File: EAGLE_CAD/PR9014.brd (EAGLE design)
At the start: 68.1 x 70.2 mm, 69 parts, among them J1 M3_SCREW_POST, SW1 C&K_PTS645

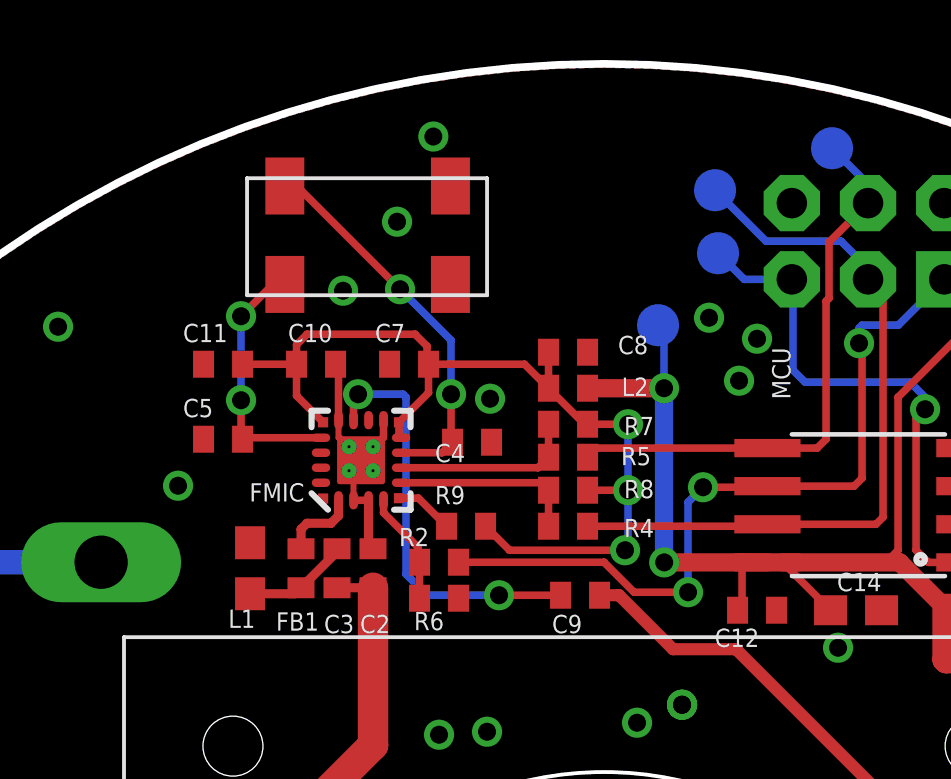
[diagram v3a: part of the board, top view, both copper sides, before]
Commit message: minor ish changes
relative to my last commit, at least

one thing that mattered a little is that i changed the XTAL package -
it was off a bit.
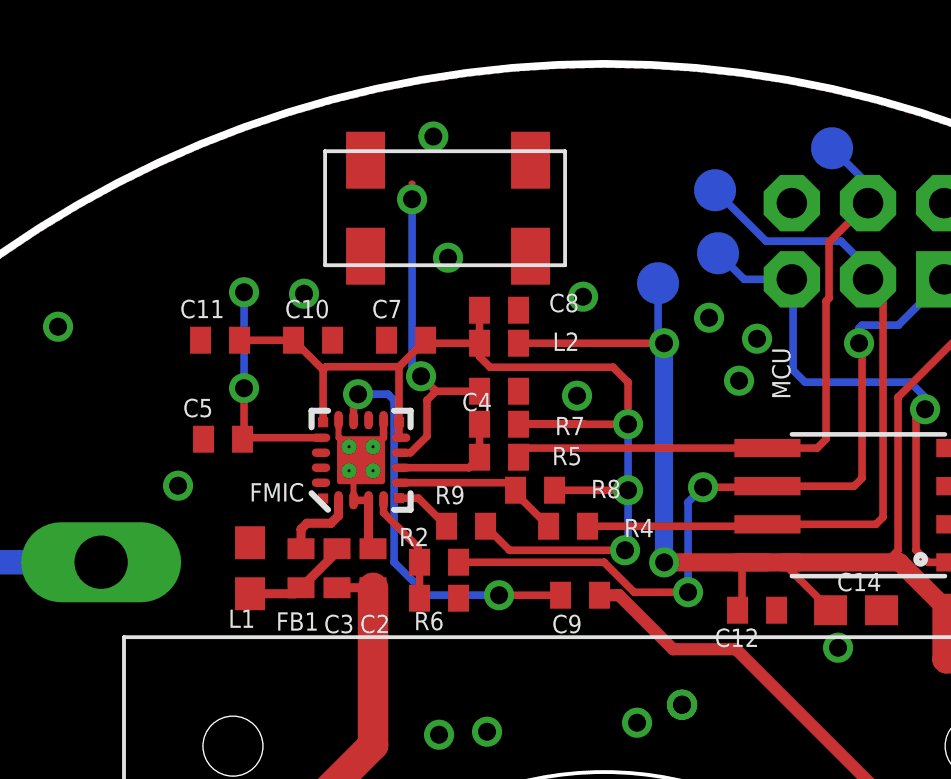
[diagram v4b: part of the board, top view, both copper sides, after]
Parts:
- moved L2 2.75 mm to (31.5, 60.8)
- moved U$6 2.72 mm to (29.8, 65.3)
- moved C8 2.69 mm to (31.5, 61.9)
- moved R5 2.30 mm to (31.5, 57.0)
- moved R7 2.30 mm to (31.5, 58.1)
- moved C4 1.92 mm to (31.5, 59.2)
- moved TP5 1.40 mm to (36.8, 62.8)
- moved R8 1.10 mm to (32.7, 55.9)
- moved C11 0.81 mm to (22.2, 60.9)
- moved C7 0.81 mm to (28.4, 60.9)
- moved C10 0.81 mm to (25.3, 60.9)
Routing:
- net 3.3V: track 32.2 -> 38.8 mm
- net VCC: track 104.9 -> 108.6 mm
- net SDIO: track 19.0 -> 21.3 mm
- net SDIO-L: track 6.16 -> 3.86 mm
- net GND: track 9.99 -> 8.23 mm, vias 41 -> 42
- net N$1: track 12.9 -> 11.4 mm
- net N$2: track 8.66 -> 7.49 mm
- net SCLK-L: track 6.22 -> 5.57 mm

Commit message: bunch of routing stuff
and made the test points larger

pretty close to being released for this round
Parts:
- added TP14, TP15, TP16, TP17, TP18: TPTP20R, testpad:TP20R
- FB2, FB3, L1: device SparkFun-Passives:0603 -> SparkFun-Passives:0805
- TP1, TP10, TP11, TP12, TP13, TP2, TP3, TP4, TP5, TP6, TP7, TP8, TP9: value TPTP14R -> TPTP20R; device testpad:TP14R -> testpad:TP20R
- moved C8 8.50 mm to (23.1, 60.6), turned to 270 degrees
- moved TP13 3.67 mm to (39.0, 68.0)
- moved U$6 2.82 mm to (27.2, 64.2)
- moved C2 2.73 mm to (24.9, 52.0), turned to 180 degrees
- moved TP11 2.02 mm to (37.0, 67.0)
- moved TP12 1.81 mm to (37.0, 64.0)
- moved TP5 1.81 mm to (37.0, 61.0)
- moved TP10 1.50 mm to (50.0, 64.0)
- moved C3 1.20 mm to (24.9, 53.2), turned to 180 degrees
- moved TP2 1.12 mm to (60.5, 35.0)
- moved FB1 1.10 mm to (24.9, 54.4), turned to 0 degrees
- moved C5 1.10 mm to (23.4, 57.6)
- moved L1 1.02 mm to (22.2, 53.5), turned to 270 degrees
- moved TP4 1.00 mm to (38.0, 17.0)
- moved TP6 1.00 mm to (26.0, 10.0)
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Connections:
- removed net N$14: C2.1, C3.1, D1.3, J1.P$1
- removed net N$15: JP5.POS, JP5.POS@2, R1.SW_OUT
- removed net N$2: C5.1, FMIC.17, U$6.P$1
- removed net N$34: FET2.3, R1.SW_IN
- new net ANT: C2.1, C3.1, D1.3, J1.P$1, TP18.TP
- new net N$10: C5.1, FMIC.17, U$6.P$4
- new net SW_IN: FET2.3, R1.SW_IN, TP14.TP
- new net SW_OUT: JP5.POS, JP5.POS@2, R1.SW_OUT, TP15.TP
- net A_IN: now also TP16.TP
- net A_OUT: now also TP17.TP
- net N$1: now also U$6.P$1; no longer U$6.P$4
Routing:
- net ANT: track 0.00 -> 38.5 mm
- net N$14: track 29.4 -> 0.00 mm
- net SW_OUT: track 0.00 -> 21.6 mm
- net N$15: track 16.1 -> 0.00 mm
- net N$10: track 0.00 -> 13.6 mm
- net SW_IN: track 0.00 -> 9.70 mm
- net N$2: track 7.49 -> 0.00 mm, vias 2 -> 0
- net N$34: track 4.20 -> 0.00 mm
- net SDIO: track 21.3 -> 25.5 mm
- net A_IN: track 35.0 -> 39.0 mm
- net A_OUT: track 38.9 -> 41.7 mm
- net SCLK: track 24.7 -> 26.9 mm
- net N$1: track 11.4 -> 13.4 mm
- net RESET: track 19.5 -> 21.4 mm
- net 3.3V: track 38.8 -> 37.3 mm
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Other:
- board size 68.1 x 70.2 mm -> 70 x 70 mm

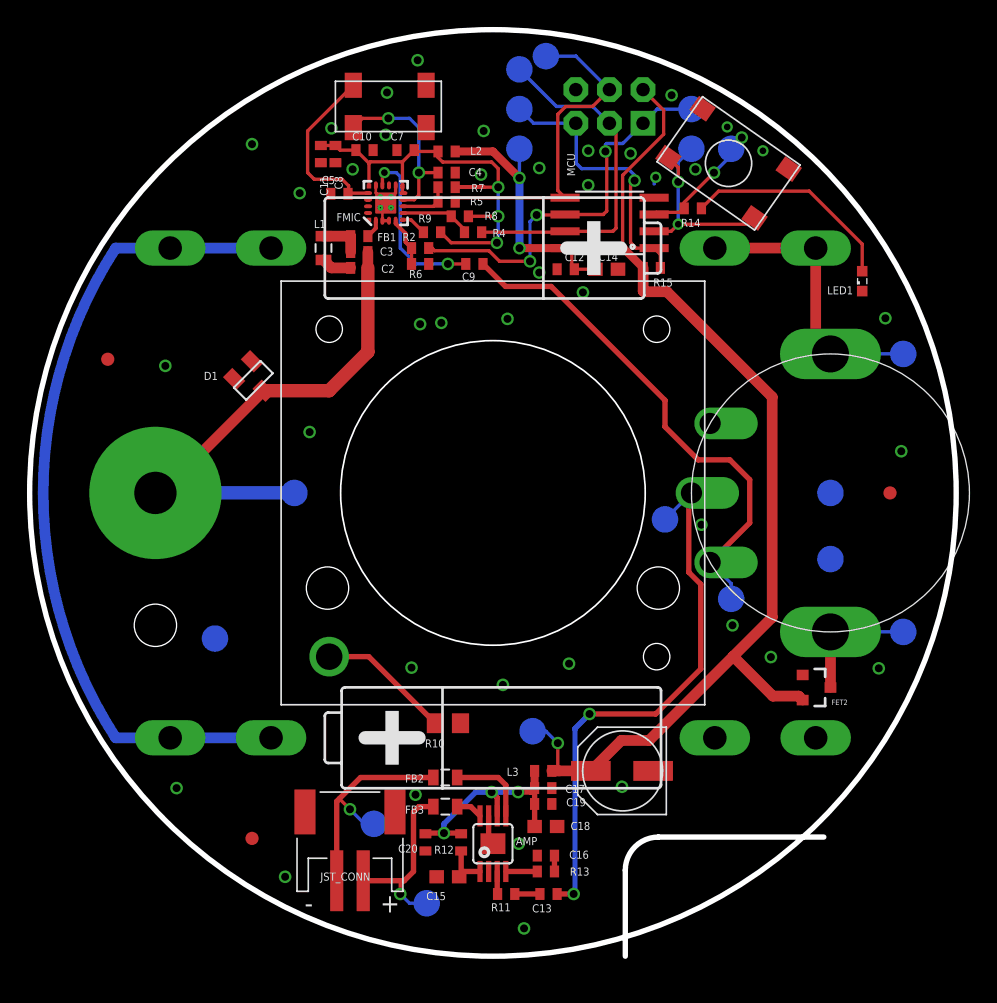
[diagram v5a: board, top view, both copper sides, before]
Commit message: Updated Layout and Library
Updated C1s package (it was a little fat)
Added vias around the edge of the board, Spk, and front end
Smoothed out a couple traces (audio, antenna test pad)
Changed battery silk to bottom layer.
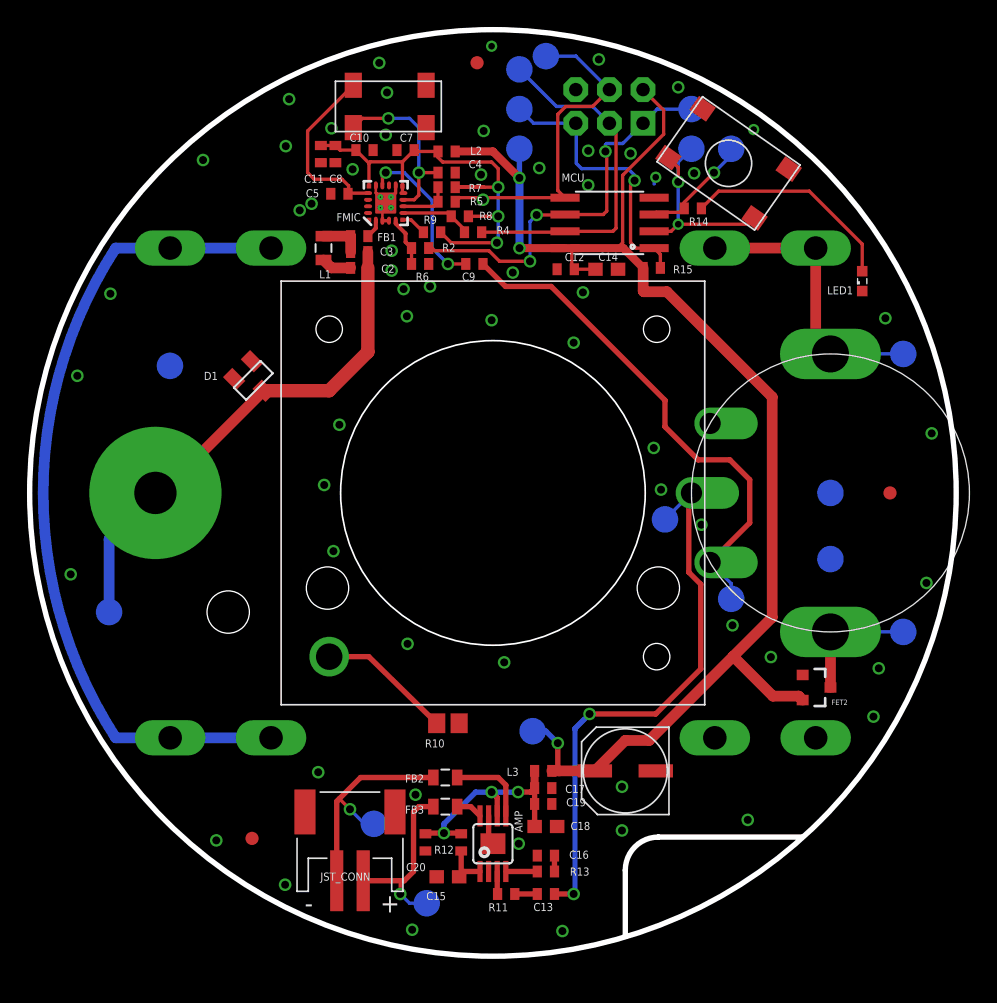
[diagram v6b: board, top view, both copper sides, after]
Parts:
- moved U$4 35.8 mm to (33.8, 67.5)
- moved TP1 20.9 mm to (10.6, 44.6)
- moved TP18 16.6 mm to (6.00, 26.0)
- moved C1 0.32 mm to (45.0, 14.0)
- moved C13 0.20 mm to (39.0, 4.70)
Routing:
- net N$9: track 13.2 -> 12.1 mm
- net GND: vias 45 -> 64
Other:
- outline, holes or cut-outs redrawn

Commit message: Updated Layout
Fixed a few things, including some notes from Andy.
Todo: change gnu pad connection on speaker screw
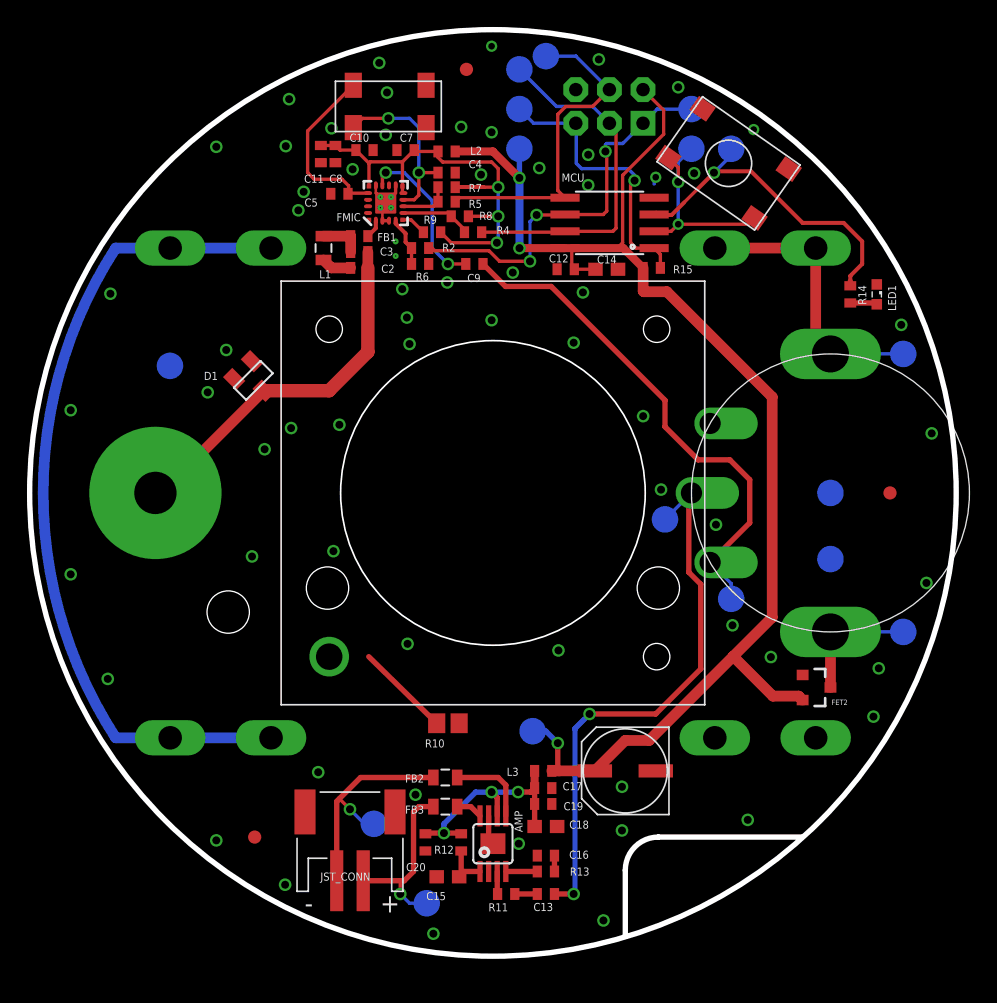
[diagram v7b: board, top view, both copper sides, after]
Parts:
- removed TP18: TPTP20R, testpad:TP20R
- moved R14 13.6 mm to (62.0, 50.0), turned to 90 degrees
- moved LED1 1.49 mm to (64.0, 50.0), turned to 270 degrees
- moved U$4 0.94 mm to (33.0, 67.0)
- moved U$3 0.22 mm to (17.0, 9.00)
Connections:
- net ANT: no longer TP18.TP
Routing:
- net LED/PB4: track 8.43 -> 25.6 mm
- net N$7: track 16.4 -> 2.04 mm
- net ANT: track 38.5 -> 28.0 mm
- net N$8: track 10.2 -> 7.18 mm
- net GND: vias 64 -> 69
